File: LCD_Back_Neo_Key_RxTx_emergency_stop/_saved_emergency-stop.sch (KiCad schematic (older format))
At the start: 11 parts, among them J6 Screw_Terminal_01x05, K1 FINDER-34.51, K2 FINDER-34.51, K3 FINDER-34.51, Q2 2N2222

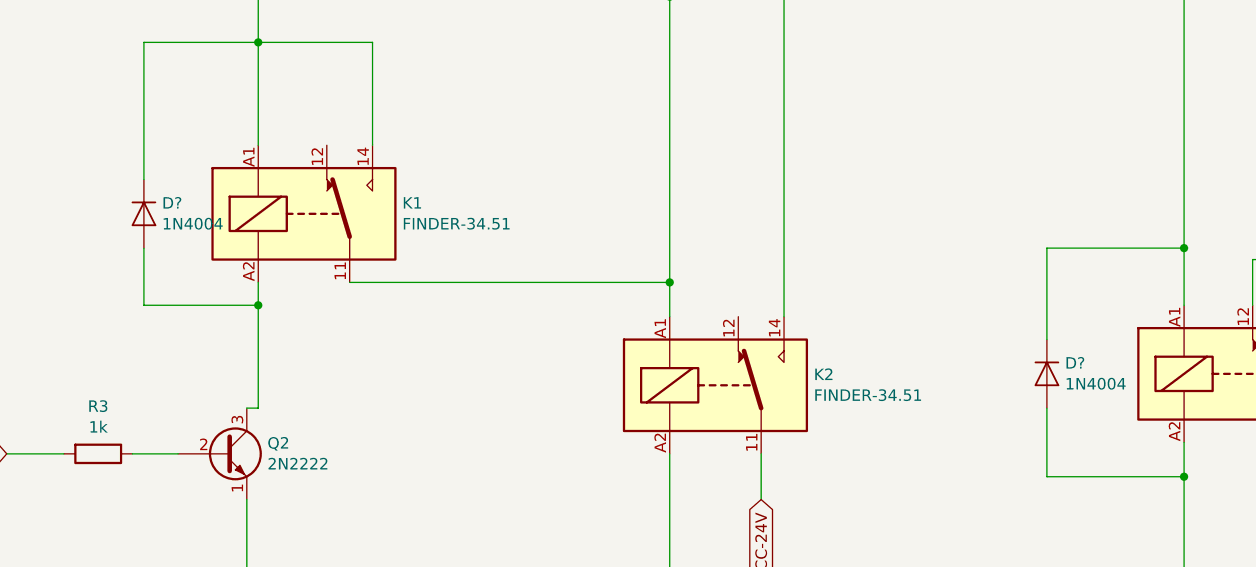
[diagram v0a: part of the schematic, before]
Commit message: add freewheeling diode for relays
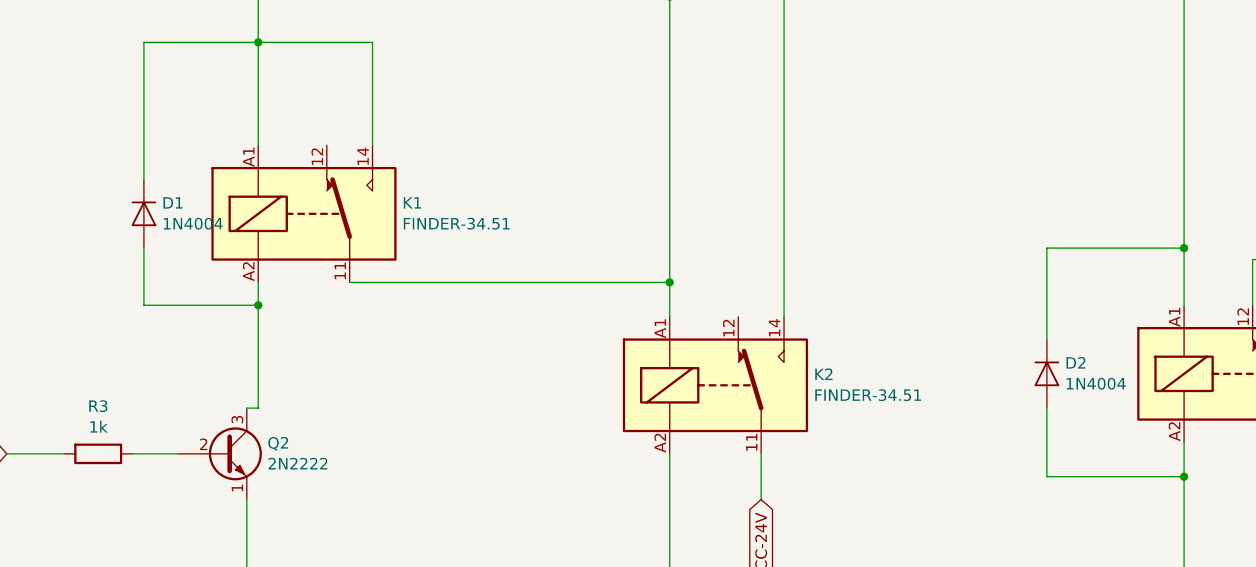
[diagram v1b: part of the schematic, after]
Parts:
- gave numbers to parts that had none: 2
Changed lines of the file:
@@
 Connection ~ 7350 3000
 $Comp
-L Diode:1N4004 D?
+L Diode:1N4004 D2
 U 1 1 5CEE427E
 P 5950 4400
-F 0 "D?" V 5904 4479 50  0000 L CNN
+F 0 "D2" V 5904 4479 50  0000 L CNN
 F 1 "1N4004" V 5995 4479 50  0000 L CNN
 F 2 "Diode_THT:D_DO-41_SOD81_P10.16mm_Horizontal" H 5950 4225 50  0001 C CNN
@@
 $EndComp
 $Comp
-L Diode:1N4004 D?
+L Diode:1N4004 D1
 U 1 1 5CEE5957
 P 2000 3700
-F 0 "D?" V 1954 3779 50  0000 L CNN
+F 0 "D1" V 1954 3779 50  0000 L CNN
 F 1 "1N4004" V 2045 3779 50  0000 L CNN
 F 2 "Diode_THT:D_DO-41_SOD81_P10.16mm_Horizontal" H 2000 3525 50  0001 C CNN
